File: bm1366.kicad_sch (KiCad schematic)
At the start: 7 parts, among them J2 Conn_01x06, U35 TXU0304PW, U8 25MHz

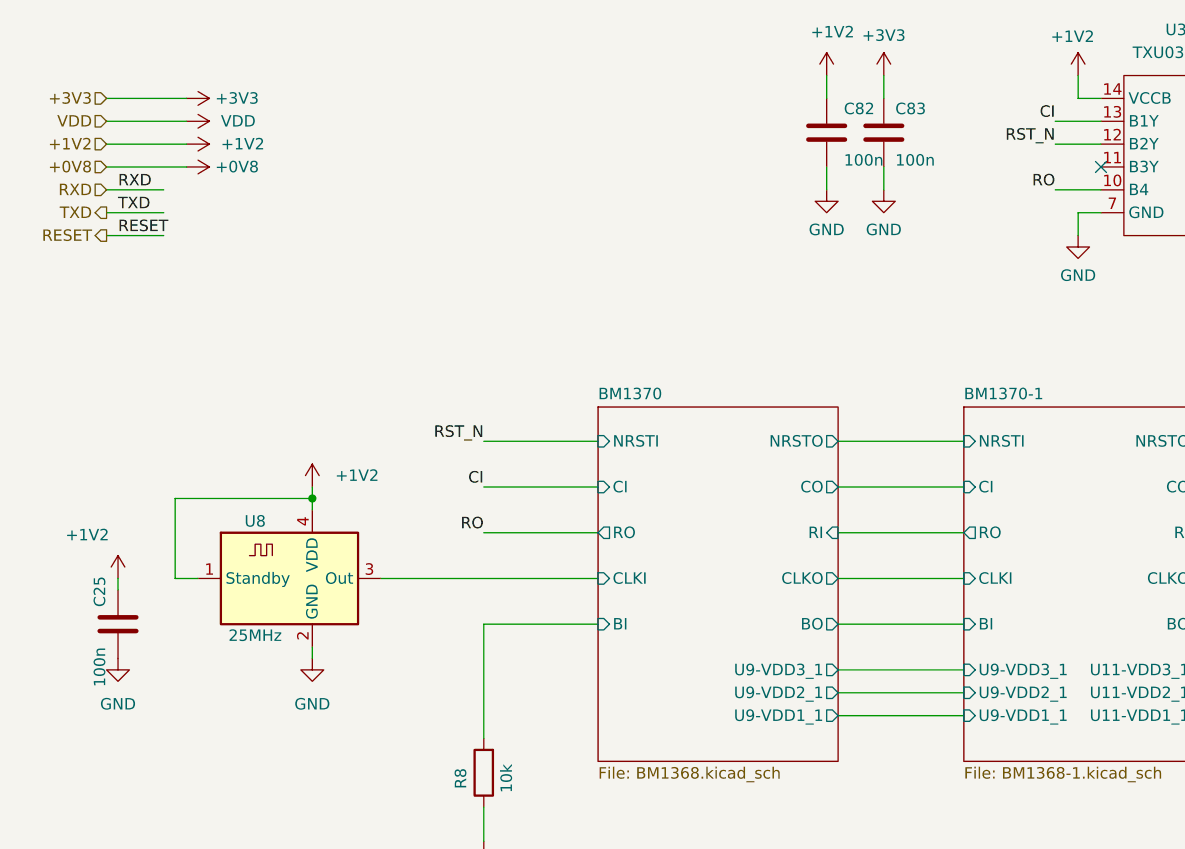
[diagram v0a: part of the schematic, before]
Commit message: BOM changes
1nF  to 1nF 0.7mm etc
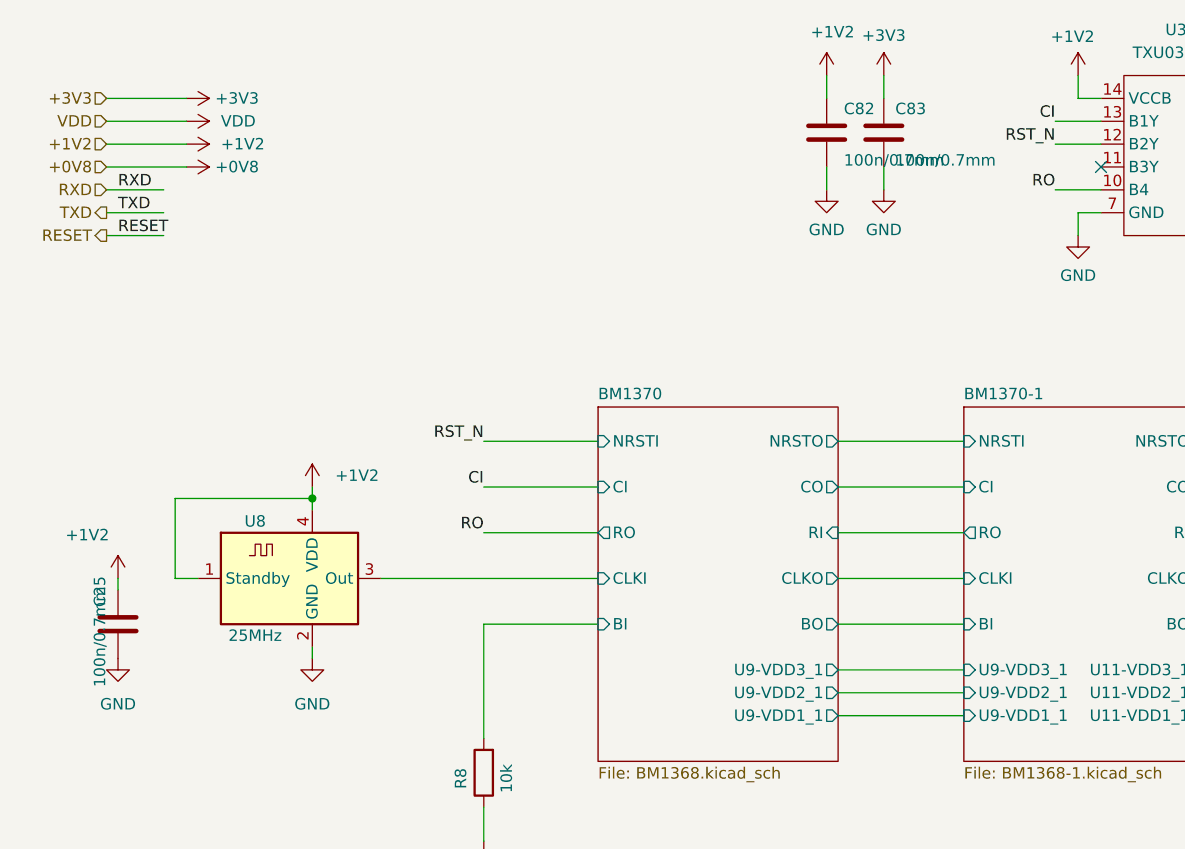
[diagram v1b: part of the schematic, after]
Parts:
- C25, C82, C83: value 100n -> 100n/0.7mm; Distributor (none) -> D; Manufacturer (none) -> AC0805KRX7R9BB104; OrderNr (none) -> 311-3037-1-ND
- R8: Distributor (none) -> D; Manufacturer (none) -> RMCF0805FT10K0; OrderNr (none) -> RMCF0805FT10K0CT-ND
- U8: Manufacturer (none) -> 1923-LFSPXO076024CT-ND
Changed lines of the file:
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@@
 			)
 		)
-		(property "Value" "100n"
+		(property "Value" "100n/0.7mm"
 			(at 116.84 39.37 0)
 			(effects
@@
 			)
 		)
+		(property "Distributor" "D"
+			(at 115.57 35.56 0)
+			(effects
+				(font
+					(size 1.27 1.27)
+				)
+				(hide yes)
+			)
+		)
+		(property "Manufacturer" "AC0805KRX7R9BB104"
+			(at 115.57 35.56 0)
+			(effects
+				(font
+					(size 1.27 1.27)
+				)
+				(hide yes)
+			)
+		)
+		(property "OrderNr" "311-3037-1-ND"
+			(at 115.57 35.56 0)
+			(effects
+				(font
+					(size 1.27 1.27)
+				)
+				(hide yes)
+			)
+		)
 		(pin "1"
 		)
@@
 			)
 		)
-		(property "Value" "100n"
+		(property "Value" "100n/0.7mm"
 			(at 29.21 97.155 90)
 			(effects
@@
 		)
 		(property "PARTNO" ""
+			(at 30.48 90.17 0)
+			(effects
+				(font
+					(size 1.27 1.27)
+				)
+				(hide yes)
+			)
+		)
+		(property "Distributor" "D"
+			(at 30.48 90.17 0)
+			(effects
+				(font
+					(size 1.27 1.27)
+				)
+				(hide yes)
+			)
+		)
+		(property "Manufacturer" "AC0805KRX7R9BB104"
+			(at 30.48 90.17 0)
+			(effects
+				(font
+					(size 1.27 1.27)
+				)
+				(hide yes)
+			)
+		)
+		(property "OrderNr" "311-3037-1-ND"
 			(at 30.48 90.17 0)
 			(effects
@@
 			)
 		)
+		(property "Manufacturer" "1923-LFSPXO076024CT-ND"
+			(at 49.53 85.09 0)
+			(effects
+				(font
+					(size 1.27 1.27)
+				)
+				(hide yes)
+			)
+		)
 		(pin "1"
 		)
@@
 			)
 		)
+		(property "Distributor" "D"
+			(at 71.12 106.68 0)
+			(effects
+				(font
+					(size 1.27 1.27)
+				)
+				(hide yes)
+			)
+		)
+		(property "Manufacturer" "RMCF0805FT10K0"
+			(at 71.12 106.68 0)
+			(effects
+				(font
+					(size 1.27 1.27)
+				)
+				(hide yes)
+			)
+		)
+		(property "OrderNr" "RMCF0805FT10K0CT-ND"
+			(at 71.12 106.68 0)
+			(effects
+				(font
+					(size 1.27 1.27)
+				)
+				(hide yes)
+			)
+		)
 		(pin "1"
 		)
@@
 			)
 		)
-		(property "Value" "100n"
+		(property "Value" "100n/0.7mm"
 			(at 111.125 39.37 0)
 			(effects
@@
 			(at 109.22 35.56 0)
 			(effects
+				(font
+					(size 1.27 1.27)
+				)
+				(hide yes)
+			)
+		)
+		(property "Distributor" "D"
+			(at 109.22 35.56 0)
+			(effects
+				(font
+					(size 1.27 1.27)
+				)
+				(hide yes)
+			)
+		)
+		(property "Manufacturer" "AC0805KRX7R9BB104"
+			(at 109.22 35.56 0)
+			(effects
+				(font
+					(size 1.27 1.27)
+				)
+				(hide yes)
+			)
+		)
+		(property "OrderNr" "311-3037-1-ND"
+			(at 109.22 35.56 0)
+			(effects

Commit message: 0502
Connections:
- net BM1370/BI renamed Asic0/BI
- net BM1370/CLKI renamed Asic0/CLKI
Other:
- removed sheet BM1370
- removed sheet BM1370-1
- removed sheet BM1370-2
- removed sheet BM1370-3
- added sheet Asic0 (Asic0.kicad_sch)
- added sheet Asic1 (Asic0.kicad_sch)
- added sheet Asic2 (Asic0.kicad_sch)
- added sheet Asic3 (Asic0.kicad_sch)
- added sheet Asic4 (Asic0.kicad_sch)
- added sheet Asic5 (Asic0.kicad_sch)
- added sheet Asic6 (Asic0.kicad_sch)
- added sheet Asic7 (Asic0.kicad_sch)
